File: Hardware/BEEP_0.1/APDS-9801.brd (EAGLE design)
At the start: 33.7 x 32.5 mm, 12 parts, among them IC1 APDS-9801

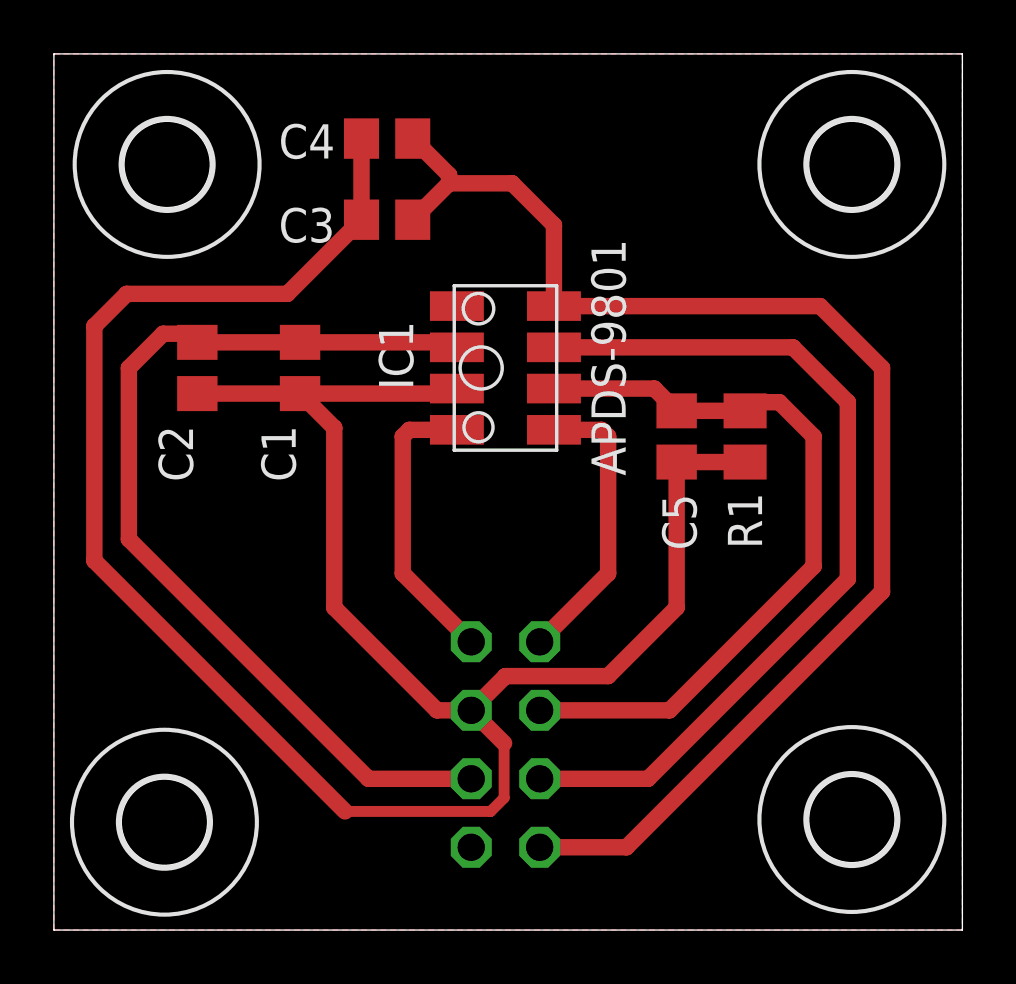
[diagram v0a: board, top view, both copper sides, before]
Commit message: enlarge Clearence to 10mil created some pdf files for the boards
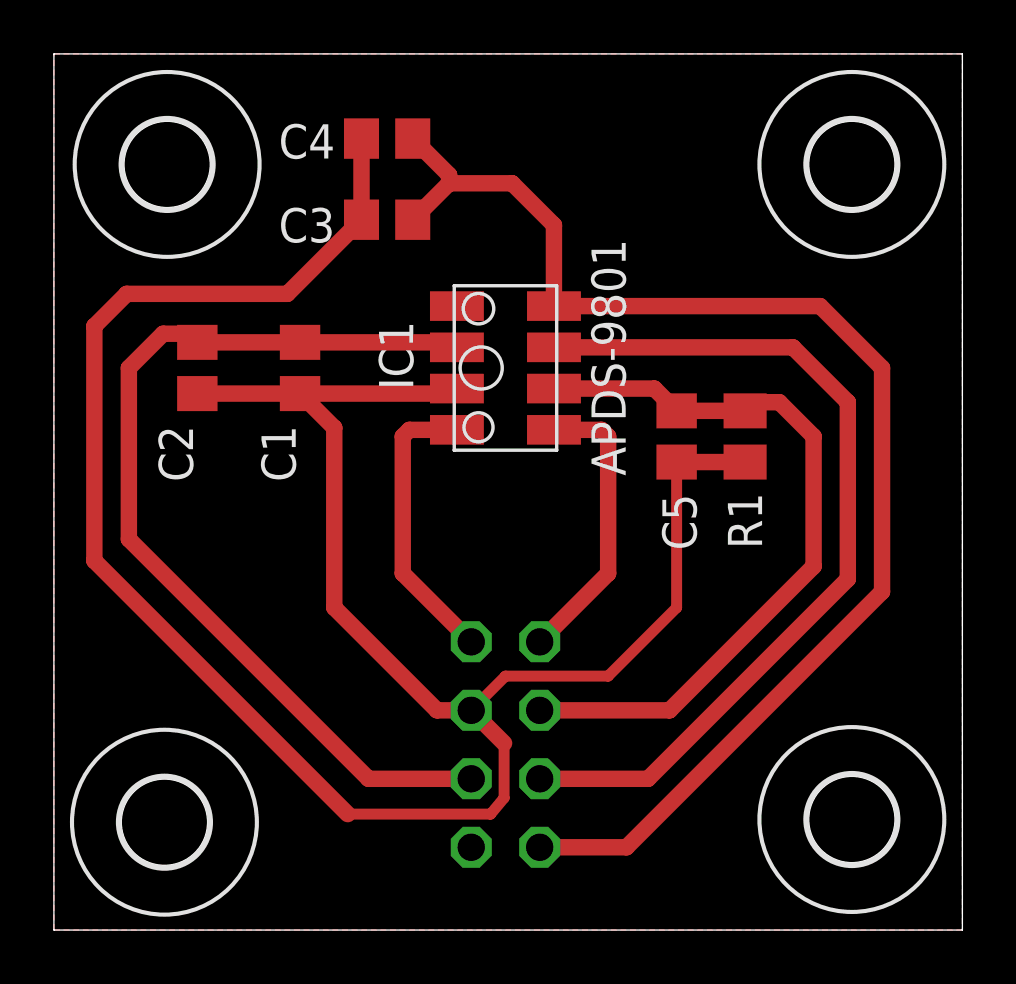
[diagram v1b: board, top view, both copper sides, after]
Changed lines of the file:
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@@
 </class>
 </classes>
-<designrules name="default">
+<designrules name="default *">
 <description language="de">&lt;b&gt;EAGLE Design Rules&lt;/b&gt;
 &lt;p&gt;
@@
 <param name="mtCopper" value="0.035mm 0.035mm 0.035mm 0.035mm 0.035mm 0.035mm 0.035mm 0.035mm 0.035mm 0.035mm 0.035mm 0.035mm 0.035mm 0.035mm 0.035mm 0.035mm"/>
 <param name="mtIsolate" value="1.5mm 0.15mm 0.2mm 0.15mm 0.2mm 0.15mm 0.2mm 0.15mm 0.2mm 0.15mm 0.2mm 0.15mm 0.2mm 0.15mm 0.2mm"/>
-<param name="mdWireWire" value="8mil"/>
-<param name="mdWirePad" value="8mil"/>
+<param name="mdWireWire" value="10mil"/>
+<param name="mdWirePad" value="10mil"/>
 <param name="mdWireVia" value="8mil"/>
 <param name="mdPadPad" value="8mil"/>
@@
 <wire x1="10.4" y1="18.63" x2="9.13" y2="19.9" width="0.6096" layer="1"/>
 <wire x1="23.1" y1="17.36" x2="25.64" y2="17.36" width="0.6096" layer="1"/>
-<wire x1="23.1" y1="17.36" x2="23.1" y2="11.96" width="0.6096" layer="1"/>
-<wire x1="23.1" y1="11.96" x2="20.56" y2="9.42" width="0.6096" layer="1"/>
-<wire x1="20.56" y1="9.42" x2="16.75" y2="9.42" width="0.6096" layer="1"/>
+<wire x1="23.1" y1="17.36" x2="23.1" y2="11.96" width="0.4064" layer="1"/>
+<wire x1="23.1" y1="11.96" x2="20.56" y2="9.42" width="0.4064" layer="1"/>
+<wire x1="20.56" y1="9.42" x2="16.75" y2="9.42" width="0.4064" layer="1"/>
 <wire x1="11.41" y1="29.36" x2="11.41" y2="26.35" width="0.6096" layer="1"/>
 <wire x1="1.5" y1="22.4" x2="1.5" y2="13.7" width="0.6096" layer="1"/>
-<wire x1="1.5" y1="13.7" x2="10.8" y2="4.4" width="0.6096" layer="1"/>
-<wire x1="10.8" y1="4.4" x2="16.2" y2="4.4" width="0.4064" layer="1"/>
-<wire x1="16.2" y1="4.4" x2="16.7" y2="4.9" width="0.4064" layer="1"/>
+<wire x1="1.5" y1="13.7" x2="10.9" y2="4.3" width="0.6096" layer="1"/>
+<wire x1="10.9" y1="4.3" x2="16.2" y2="4.3" width="0.4064" layer="1"/>
+<wire x1="16.2" y1="4.3" x2="16.7" y2="4.9" width="0.4064" layer="1"/>
 <wire x1="16.7" y1="4.9" x2="16.7" y2="6.93" width="0.4064" layer="1"/>
 <polygon width="0.6096" layer="1">
@@
 <contactref element="JP1" pad="4"/>
 <wire x1="14.21" y1="8.15" x2="15.48" y2="8.15" width="0.6096" layer="1"/>
-<wire x1="16.75" y1="9.42" x2="15.48" y2="8.15" width="0.6096" layer="1"/>
+<wire x1="16.75" y1="9.42" x2="15.48" y2="8.15" width="0.4064" layer="1"/>
 <wire x1="15.48" y1="8.15" x2="16.7" y2="6.93" width="0.6096" layer="1"/>
 </signal>

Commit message: Add branding ;) enhance PCBs finish Easy RGB Board add Texas Instruments libray from Element 14 add dxf import ulp for eagle add Script for easy eagle export to pdf for etching minor cleanup
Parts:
- removed U$2: (no value), holes:3,2
- added U$1: (no value), Branding:COPPER4
- C1, C3, C5: device rcl:C0805 -> rcl:C025-024X044
- moved C2 5.40 mm to (10.7, 20.8)
- moved C4 3.41 mm to (12.6, 26.0)
- moved C3 2.61 mm to (12.6, 28.9), flipped to the bottom, turned to 0 degrees
- moved C1 1.30 mm to (7.87, 20.6), flipped to the bottom
- moved C5 0.22 mm to (23.3, 18.4), flipped to the bottom
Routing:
- net GND: track 88.4 -> 80.3 mm
- net VCC: track 35.6 -> 30.3 mm
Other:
- board text added: "APDS-9801 v0.2"
